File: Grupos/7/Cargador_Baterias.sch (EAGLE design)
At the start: 48 parts, among them M1 NUCLEO-L452RE, U1 MCP73830T-2AAI/MYY, U2 MCP73830T-2AAI/MYY, U3 MCP73830T-2AAI/MYY

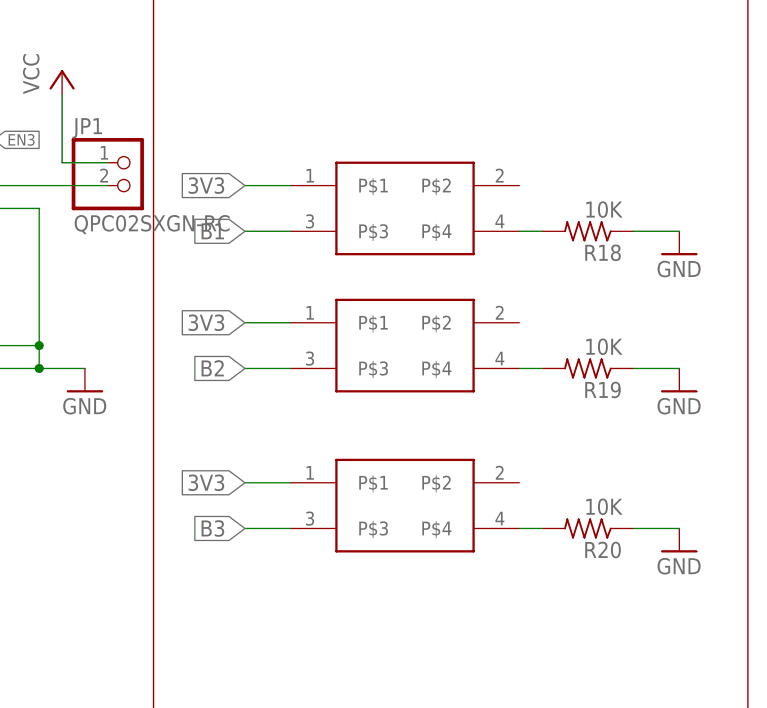
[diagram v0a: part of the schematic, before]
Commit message: Se arregla botón
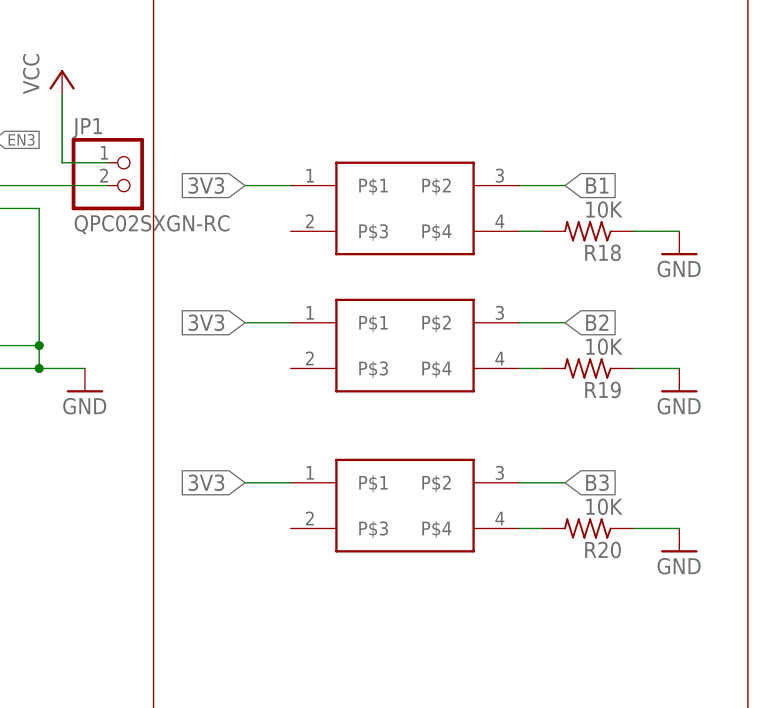
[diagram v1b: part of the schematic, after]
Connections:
- net B1: now also BOTON1.P$2; no longer BOTON1.P$3
- net B2: now also BOTON2.P$2; no longer BOTON2.P$3
- net B3: now also BOTON3.P$2; no longer BOTON3.P$3
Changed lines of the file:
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@@
 <drawing>
 <settings>
-<setting alwaysvectorfont="no"/>
+<setting alwaysvectorfont="yes"/>
 <setting verticaltext="up"/>
 </settings>
@@
 <net name="B1" class="0">
 <segment>
-<pinref part="BOTON1" gate="G$1" pin="P$3"/>
-<wire x1="144.78" y1="134.62" x2="139.7" y2="134.62" width="0.1524" layer="91"/>
-<label x="139.7" y="134.62" size="1.778" layer="95" rot="MR0" xref="yes"/>
-</segment>
-<segment>
 <pinref part="M1" gate="-CN9" pin="PB10"/>
 <wire x1="-5.08" y1="129.54" x2="-10.16" y2="129.54" width="0.1524" layer="91"/>
 <label x="-10.16" y="129.54" size="1.27" layer="95" rot="MR0" xref="yes"/>
 </segment>
+<segment>
+<wire x1="170.18" y1="139.7" x2="175.26" y2="139.7" width="0.1524" layer="91"/>
+<label x="175.26" y="139.7" size="1.778" layer="95" rot="MR180" xref="yes"/>
+<pinref part="BOTON1" gate="G$1" pin="P$2"/>
+</segment>
 </net>
 <net name="B2" class="0">
-<segment>
-<pinref part="BOTON2" gate="G$1" pin="P$3"/>
-<wire x1="144.78" y1="119.38" x2="139.7" y2="119.38" width="0.1524" layer="91"/>
-<label x="139.7" y="119.38" size="1.778" layer="95" rot="MR0" xref="yes"/>
-</segment>
 <segment>
 <pinref part="M1" gate="-CN9" pin="PA8"/>
@@
 <label x="-10.16" y="127" size="1.27" layer="95" rot="MR0" xref="yes"/>
 </segment>
+<segment>
+<wire x1="170.18" y1="124.46" x2="175.26" y2="124.46" width="0.1524" layer="91"/>
+<label x="175.26" y="124.46" size="1.778" layer="95" rot="MR180" xref="yes"/>
+<pinref part="BOTON2" gate="G$1" pin="P$2"/>
+</segment>
 </net>
 <net name="B3" class="0">
-<segment>
-<pinref part="BOTON3" gate="G$1" pin="P$3"/>
-<wire x1="144.78" y1="101.6" x2="139.7" y2="101.6" width="0.1524" layer="91"/>
-<label x="139.7" y="101.6" size="1.778" layer="95" rot="MR0" xref="yes"/>
-</segment>
 <segment>
 <pinref part="M1" gate="-CN9" pin="PB4"/>
@@
 <label x="-10.16" y="132.08" size="1.27" layer="95" rot="MR0" xref="yes"/>
 </segment>
-</net>
+<segment>
+<wire x1="170.18" y1="106.68" x2="175.26" y2="106.68" width="0.1524" layer="91"/>
+<label x="175.26" y="106.68" size="1.778" layer="95" rot="MR180" xref="yes"/>
+<pinref part="BOTON3" gate="G$1" pin="P$2"/>
+</segment>
+</net>
